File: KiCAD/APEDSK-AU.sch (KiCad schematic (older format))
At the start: 25 parts, among them J1 240-44-44Pins, P1 Power, P2 Analog, P3 Digital, P4 Digital, U1 74LS245, U2 74LS541, U3 74LS541, U4 74LS138, U5 74HC595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

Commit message: Added R5 for D2:TI_INT/ETH_CS shared use
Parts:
- added R5: 1K, Resistor_THT:R_Axial_DIN0204_L3.6mm_D1.6mm_P5.08mm_Vertical, symbol Device:R_Small_US
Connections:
- net ~TI_INT: now also R5.1; no longer U4.15 (O0)
- new net: R5.2, U4.15 (O0)
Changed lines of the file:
@@
 	7050 3050 6100 3050
-Wire Wire Line
-	6100 3050 6100 5250
 Wire Wire Line
 	6100 5250 6800 5250
@@
 Text Label 5800 6750 2    50   ~ 0
 A15
+$Comp
+L Device:R_Small_US R5
+U 1 1 5F4050AD
+P 6100 4150
+F 0 "R5" H 6168 4196 50  0000 L CNN
+F 1 "1K" H 6168 4105 50  0000 L CNN
+F 2 "Resistor_THT:R_Axial_DIN0204_L3.6mm_D1.6mm_P5.08mm_Vertical" H 6100 4150 50  0001 C CNN
+F 3 "~" H 6100 4150 50  0001 C CNN
+	1    6100 4150
+	1    0    0    -1
+$EndComp
+Wire Wire Line
+	6100 3050 6100 4050
+Wire Wire Line
+	6100 4250 6100 5250
 $EndSCHEMATC

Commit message: added R6 noise supression resistor
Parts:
- added R6: 1K, Resistor_THT:R_Axial_DIN0204_L3.6mm_D1.6mm_P5.08mm_Vertical, symbol Device:R_Small_US
- D2: value 1N5711 -> 1N4148
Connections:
- net READY: now also R6.2; no longer D2.2 (A)
- new net: D2.2 (A), R6.1
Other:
- moved on the sheet: R5
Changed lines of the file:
@@
 	-1   0    0    -1
 $EndComp
-Text Label 6600 3450 2    50   ~ 0
+Text Label 6250 3450 2    50   ~ 0
 READY
 NoConn ~ 4800 6950
@@
 P 6800 3450
 F 0 "D2" H 6800 3655 50  0000 C CNN
-F 1 "1N5711" H 6800 3564 50  0000 C CNN
+F 1 "1N4148" H 6800 3564 50  0000 C CNN
 F 2 "Diode_THT:D_A-405_P5.08mm_Vertical_AnodeUp" V 6800 3450 50  0001 C CNN
 F 3 "~" V 6800 3450 50  0001 C CNN
@@
 Wire Wire Line
 	7050 3350 7050 3050
-Wire Wire Line
-	7050 3050 6100 3050
-Wire Wire Line
-	6100 5250 6800 5250
 Wire Wire Line
 	6800 5250 6800 6250
@@
 L Device:R_Small_US R5
 U 1 1 5F4050AD
-P 6100 4150
-F 0 "R5" H 6168 4196 50  0000 L CNN
-F 1 "1K" H 6168 4105 50  0000 L CNN
-F 2 "Resistor_THT:R_Axial_DIN0204_L3.6mm_D1.6mm_P5.08mm_Vertical" H 6100 4150 50  0001 C CNN
-F 3 "~" H 6100 4150 50  0001 C CNN
-	1    6100 4150
-	1    0    0    -1
-$EndComp
-Wire Wire Line
-	6100 3050 6100 4050
-Wire Wire Line
-	6100 4250 6100 5250
+P 5850 4150
+F 0 "R5" H 5918 4196 50  0000 L CNN
+F 1 "1K" H 5918 4105 50  0000 L CNN
+F 2 "Resistor_THT:R_Axial_DIN0204_L3.6mm_D1.6mm_P5.08mm_Vertical" H 5850 4150 50  0001 C CNN
+F 3 "~" H 5850 4150 50  0001 C CNN
+	1    5850 4150
+	1    0    0    -1
+$EndComp
+Wire Wire Line
+	5850 3050 5850 4050
+Wire Wire Line
+	5850 4250 5850 5250
+$Comp
+L Device:R_Small_US R6
+U 1 1 5F54C1B7
+P 6500 3450
+F 0 "R6" V 6400 3400 50  0000 L CNN
+F 1 "1K" V 6600 3400 50  0000 L CNN
+F 2 "Resistor_THT:R_Axial_DIN0204_L3.6mm_D1.6mm_P5.08mm_Vertical" H 6500 3450 50  0001 C CNN
+F 3 "~" H 6500 3450 50  0001 C CNN
+	1    6500 3450
+	0    1    1    0
+$EndComp
+Wire Wire Line
+	5850 3050 7050 3050
+Wire Wire Line
+	5850 5250 6800 5250
+Wire Wire Line
+	6250 3450 6400 3450
 $EndSCHEMATC

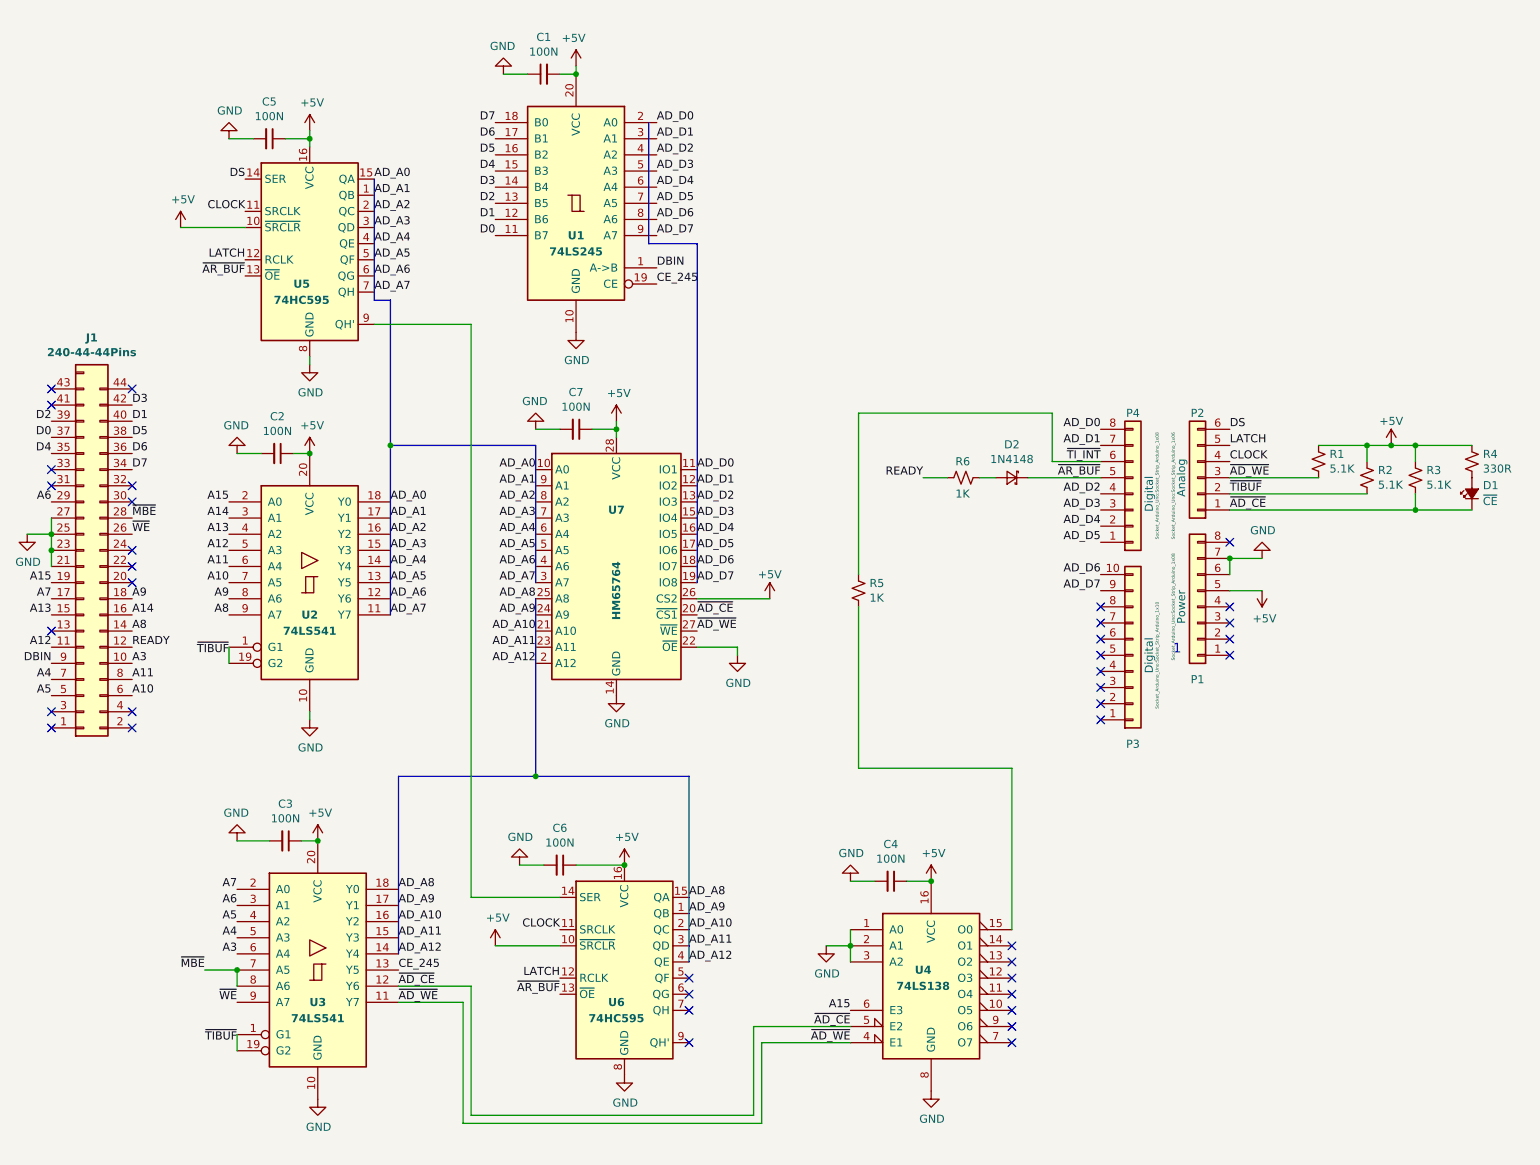
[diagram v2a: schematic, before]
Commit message: APEETH99 -> APEDSK99
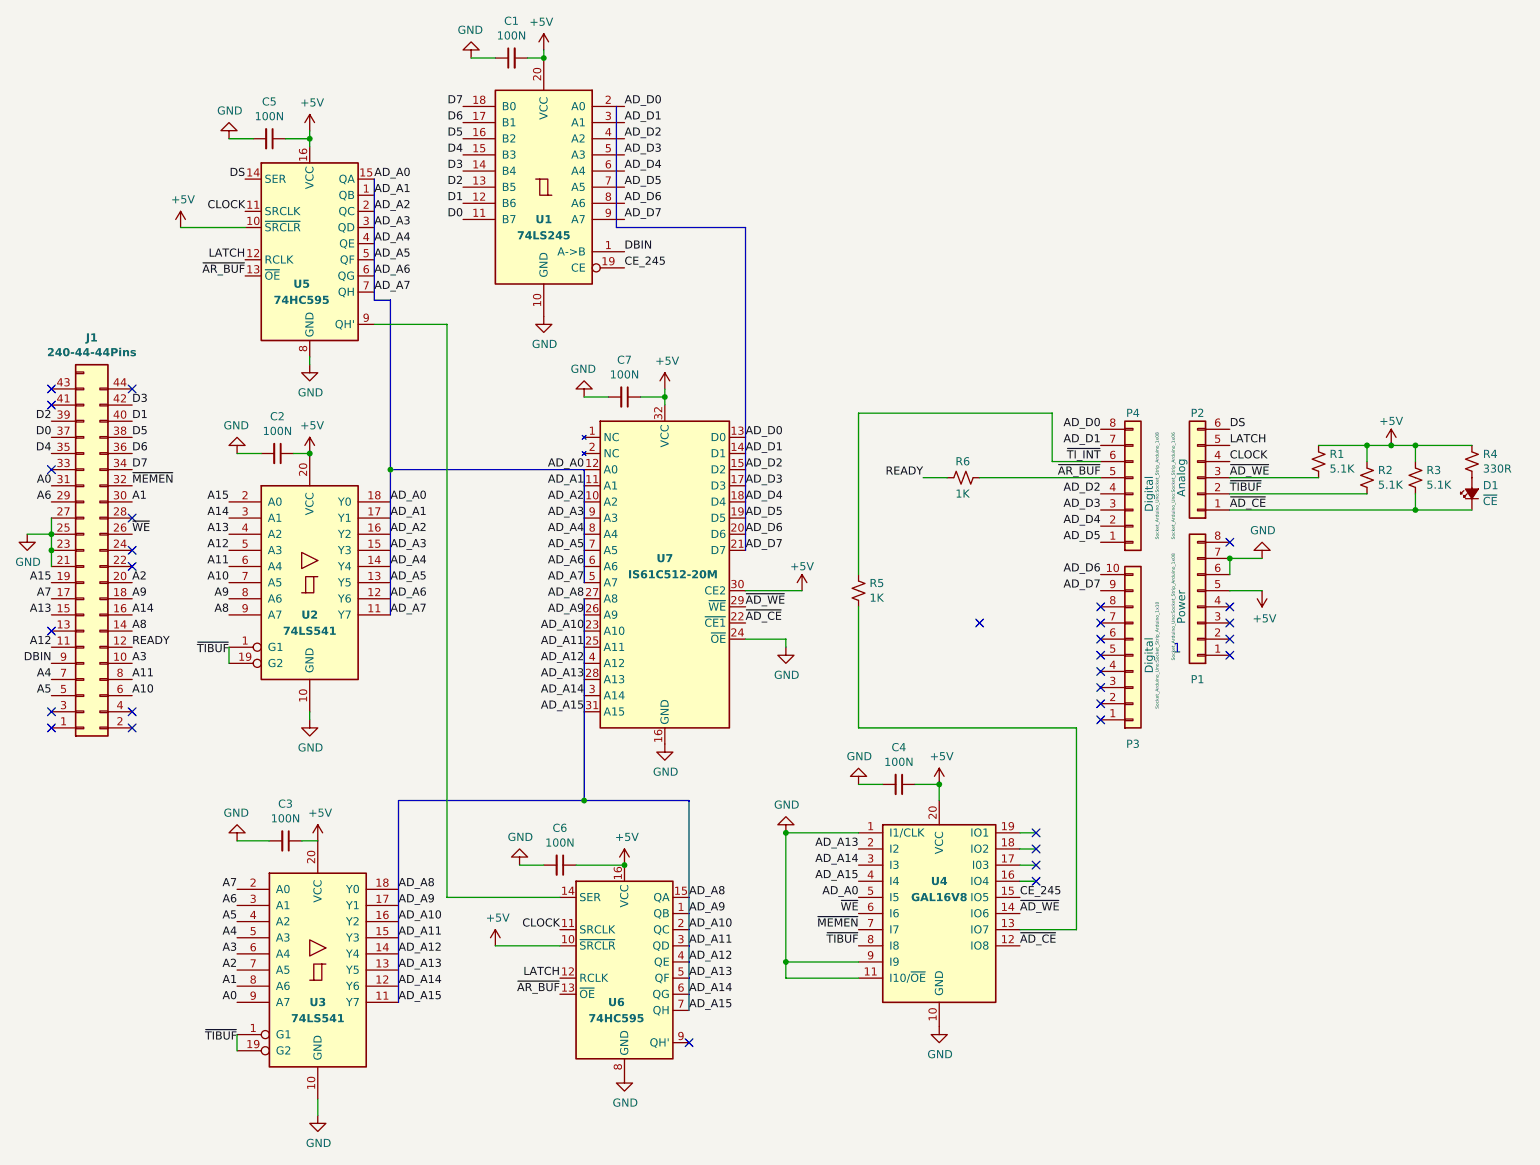
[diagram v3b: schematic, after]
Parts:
- removed D2: 1N4148, Diode_THT:D_A-405_P5.08mm_Vertical_AnodeUp, symbol Device:D_Schottky_Small
- removed U4: 74LS138, Package_DIP:DIP-16_W7.62mm, symbol 74xx:74LS138
- removed U7: HM65764, Package_DIP:DIP-28_W7.62mm, symbol Memory_RAM:6264ALP_DIP32_SSOP32
- added U4: GAL16V8, Package_DIP:DIP-20_W7.62mm, symbol Logic_Programmable:GAL16V8
- added U7: IS61C512-20M, Package_DIP:DIP-32_W7.62mm, symbol Memory_RAM:IS61C512-20M
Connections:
- net +5V: now also U4.20 (VCC), U7.30 (CE2), U7.32 (VCC)
- net AD_A0: now also U4.5 (I5), U7.12 (A0)
- net AD_A1: now also U7.11 (A1)
- net AD_A10: now also U7.23 (A10)
- net AD_A11: now also U7.25 (A11)
- net AD_A12: now also U7.4 (A12)
- net AD_A2: now also U7.10 (A2)
- net AD_A3: now also U7.9 (A3)
- net AD_A4: now also U7.8 (A4)
- net AD_A5: now also U7.7 (A5)
- net AD_A6: now also U7.6 (A6)
- net AD_A7: now also U7.5 (A7)
- net AD_A8: now also U7.27 (A8)
- net AD_A9: now also U7.26 (A9)
- net AD_D0: now also U7.13 (D0)
- net AD_D1: now also U7.14 (D1)
- net AD_D2: now also U7.15 (D2)
- net AD_D3: now also U7.17 (D3)
- net AD_D4: now also U7.18 (D4)
- net AD_D5: now also U7.19 (D5)
- net AD_D6: now also U7.20 (D6)
- net AD_D7: now also U7.21 (D7)
- net CE_245: now also U4.15 (IO5); no longer U3.13 (Y5)
- net GND: now also U4.1 (I1/CLK), U4.10 (GND), U4.11 (I10/~OE~), U4.9 (I9), U7.16 (GND), U7.24 (~OE)
- net ~AD_CE: now also U4.12 (IO8), U7.22 (~CE1); no longer U3.12 (Y6)
- net ~AD_WE: now also U4.14 (IO6), U7.29 (~WE); no longer U3.11 (Y7)
- net ~AR_BUF: now also R6.1
- net ~TIBUF: now also U4.8 (I8)
- net ~WE: now also U4.6 (I6); no longer U3.9 (A7)
- net A2: now reaches J1.20 (Pin_20)
- net A2: now also U3.7 (A5)
- net A1: now reaches J1.30 (Pin_30)
- net A1: now also U3.8 (A6)
- net A0: now reaches J1.31 (Pin_31)
- net A0: now also U3.9 (A7)
- net ~MEMEN: now reaches J1.32 (Pin_32)
- net ~MEMEN: now also U4.7 (I7)
- net AD_A13: now reaches U6.5 (QF)
- net AD_A13: now also U3.13 (Y5), U4.2 (I2), U7.28 (A13)
- net AD_A14: now reaches U6.6 (QG)
- net AD_A14: now also U3.12 (Y6), U4.3 (I3), U7.3 (A14)
- net AD_A15: now reaches U6.7 (QH)
- net AD_A15: now also U3.11 (Y7), U4.4 (I4), U7.31 (A15)
- net at R5.2: now also U4.13 (IO7)
- removed net ~MBE: J1.28 (Pin_28), U3.7 (A5), U3.8 (A6)
- no-connect marks 39 -> 31
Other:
- moved on the sheet: C1, C4, C7, U1
